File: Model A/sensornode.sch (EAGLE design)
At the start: 31 parts, among them U1 ATMEGA328P_PDIP

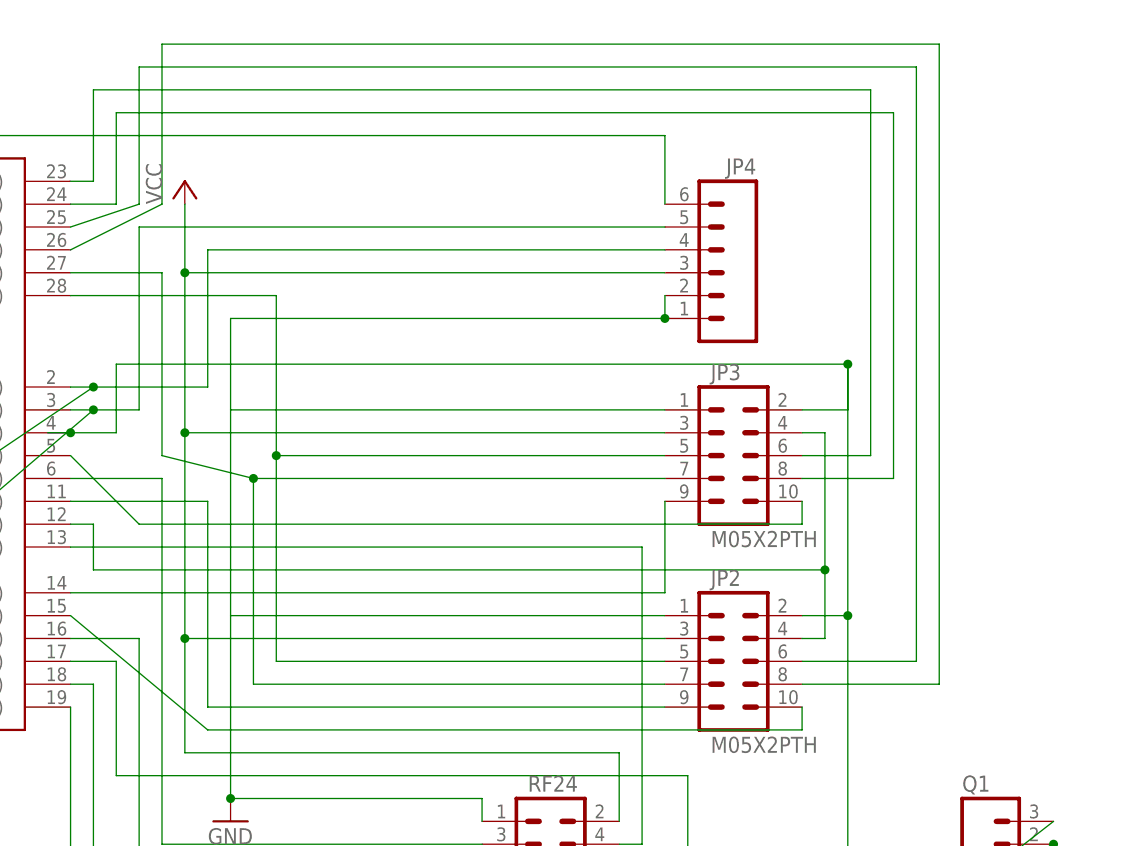
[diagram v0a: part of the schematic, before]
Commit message: fixed sensornode radio direction, power pin labels
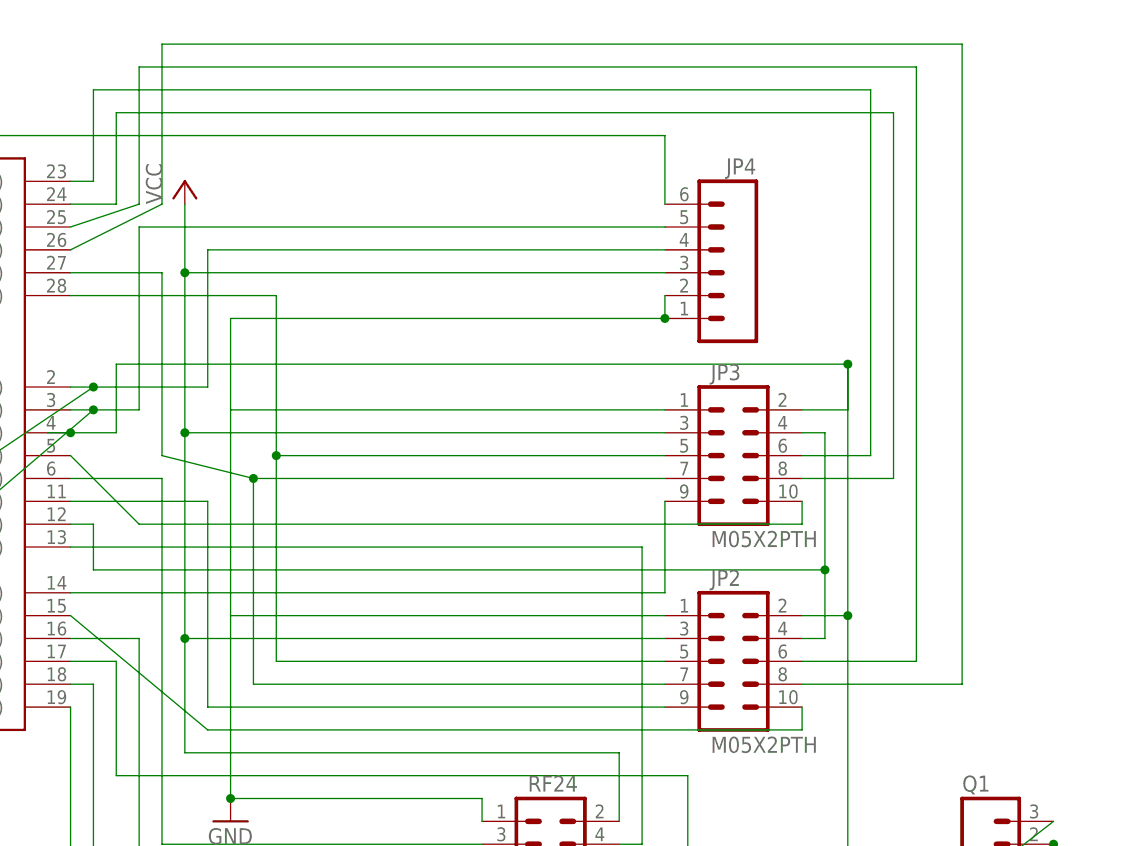
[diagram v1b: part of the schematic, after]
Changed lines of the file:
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@@
 <wire x1="2.54" y1="55.88" x2="12.7" y2="60.96" width="0.1524" layer="91"/>
 <wire x1="12.7" y1="60.96" x2="12.7" y2="78.74" width="0.1524" layer="91"/>
-<wire x1="12.7" y1="78.74" x2="99.06" y2="78.74" width="0.1524" layer="91"/>
-<wire x1="99.06" y1="78.74" x2="99.06" y2="7.62" width="0.1524" layer="91"/>
+<wire x1="12.7" y1="78.74" x2="101.6" y2="78.74" width="0.1524" layer="91"/>
+<wire x1="101.6" y1="78.74" x2="101.6" y2="7.62" width="0.1524" layer="91"/>
 <pinref part="JP2" gate="G$1" pin="8"/>
-<wire x1="83.82" y1="7.62" x2="99.06" y2="7.62" width="0.1524" layer="91"/>
+<wire x1="83.82" y1="7.62" x2="101.6" y2="7.62" width="0.1524" layer="91"/>
 </segment>
 </net>
